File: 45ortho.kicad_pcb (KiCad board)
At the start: 2 copper layers, 266.7 x 95.2 mm, 158 parts

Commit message: a bit update (few routing, pro micro added, rotary added)
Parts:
- removed the REF** at (222.2, 146.1)
- removed the REF** at (210.3, 146.1)
- removed the REF** at (141.3, 146.1)
- removed the REF** at (117.5, 146.1)
- removed the REF** at (93.7, 146.1)
- removed the REF** at (138.9, 146.1)
- removed the REF** at (115.1, 146.1)
- removed the REF** at (91.3, 146.1)
- added D63: 1N4148W, Keebio-Parts:Diode-dual - Copy, B.Cu at (217.5, 146.1)
- added J1: ProMicro Extra Pin, Connector_PinSocket_2.54mm:PinSocket_1x02_P2.54mm_Vertical, B.Cu at (222.2, 144.8)
- added J2: USB Header, Connector_PinSocket_2.54mm:PinSocket_1x04_P2.54mm_Vertical, F.Cu at (151.8, 98.4)
- added MX63: MX-NoLED, MX_Only:MXOnly-1U-NoLED, F.Cu at (203.2, 146.1)
- added R1: 5.1k, Resistor_SMD:R_0603_1608Metric, B.Cu at (100.8, 88.9)
- added R2: 5.1k, Resistor_SMD:R_0603_1608Metric, B.Cu at (96.0, 88.9)
- added R3: 5.1k, Resistor_SMD:R_0603_1608Metric, B.Cu at (100.8, 69.8)
- added R4: 5.1k, Resistor_SMD:R_0603_1608Metric, B.Cu at (96.0, 69.8)
- added REF**: RotaryEncoder_EC11, Keebio-Parts:RotaryEncoder_EC11, B.Cu at (336.8, 69.8)
- added U3: ProMicro, Keebio-Parts:ArduinoProMicro-TopSide, B.Cu at (193.7, 146.1)
- added USB1: 6x14, Keebio-Parts:HRO-TYPE-C-31-M-12-Assembly, B.Cu at (98.4, 77.2)
- added USB2: 5x14, Keebio-Parts:HRO-TYPE-C-31-M-12-Assembly, B.Cu at (98.4, 57.9)
- MX62: footprint MX_Only:MXOnly-1U-NoLED -> MX_Only:MXOnly-6U-Centered-ReversedStabilizers-NoLED
- moved D61 30.7 mm to (214.3, 146.1), turned to 270 degrees
- moved D14 11.2 mm to (326.0, 71.5), turned to 270 degrees
- moved D62 9.69 mm to (211.1, 146.1), turned to 270 degrees
- moved MX62 9.52 mm to (193.7, 146.1)
- moved D59 7.94 mm to (127.0, 151.6)
- moved D44 1.40 mm to (108.0, 132.6)
- renumbered D63 to D64, D64 to D65, D65 to D66, D66 to D67, D67 to D68, D68 to D69, MX63 to MX64, MX64 to MX65, MX65 to MX66, MX66 to MX67, MX67 to MX68, MX68 to MX69
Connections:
- MX60 pad 1: col3 -> col4
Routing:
- net GND: track 0.00 -> 403.2 mm, vias 0 -> 2
- net row4: track 0.00 -> 311.4 mm
- net row1: track 0.00 -> 264.2 mm
- net row3: track 0.00 -> 263.2 mm
- net row2: track 0.00 -> 263.2 mm
- net D+: track 0.00 -> 177.5 mm, vias 0 -> 2
- net +5V: track 0.00 -> 167.5 mm, vias 0 -> 5
- net D-: track 0.00 -> 157.3 mm, vias 0 -> 2
- net col13: track 21.9 -> 112.8 mm
- net col8: track 21.8 -> 91.9 mm
- net col11: track 21.8 -> 82.1 mm
- net col12: track 21.8 -> 81.9 mm
- net col10: track 21.8 -> 81.8 mm
- net col9: track 21.8 -> 81.8 mm
- net col2: track 21.8 -> 81.8 mm
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- added copper zone on B.Cu, net GND
- added copper zone on F.Cu, net GND
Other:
- board text added: "+"
- board text added: "-"
- board text added: "G"
- board text added: "V"

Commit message: 99.99% final
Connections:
- J1 pad 1: (no net) -> row0
- U3 pad 1: (no net) -> col4
- U3 pad 10: (no net) -> col11
- U3 pad 11: (no net) -> col10
- U3 pad 12: (no net) -> col9
- U3 pad 13: (no net) -> row3
- U3 pad 14: (no net) -> row2
- U3 pad 15: (no net) -> row1
- U3 pad 16: (no net) -> row4
- U3 pad 17: (no net) -> col3
- U3 pad 18: (no net) -> col2
- U3 pad 19: (no net) -> col1
- U3 pad 2: (no net) -> col5
- U3 pad 20: (no net) -> col0
- U3 pad 5: (no net) -> col6
- U3 pad 6: (no net) -> col7
- U3 pad 7: (no net) -> col8
- U3 pad 8: (no net) -> col13
- U3 pad 9: (no net) -> col12
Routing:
- net col13: track 112.8 -> 259.3 mm
- net col12: track 81.9 -> 206.4 mm
- net col0: track 85.3 -> 198.4 mm
- net col11: track 82.1 -> 189.0 mm
- net row0: track 257.6 -> 360.4 mm, vias 0 -> 1
- net col1: track 81.8 -> 178.0 mm
- net col3: track 61.8 -> 145.3 mm
- net col10: track 81.8 -> 165.2 mm
- net row1: track 264.2 -> 346.0 mm, vias 0 -> 2
- net col2: track 81.8 -> 161.3 mm
- net row2: track 263.2 -> 327.5 mm, vias 0 -> 2
- net col9: track 81.8 -> 142.9 mm
- net col7: track 61.8 -> 112.6 mm
- net row3: track 263.2 -> 310.0 mm, vias 0 -> 1
- net col8: track 91.9 -> 128.1 mm
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
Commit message: bit of update
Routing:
- net GND: vias 19 -> 20
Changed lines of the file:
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@@
     (thickness 1.6)
     (drawings 8)
-    (tracks 972)
+    (tracks 973)
     (zones 0)
     (modules 162)
@@
     (add_net "Net-(D8-Pad2)")
     (add_net "Net-(D9-Pad2)")
-    (add_net "Net-(J1-Pad2)")
     (add_net "Net-(R1-Pad1)")
     (add_net "Net-(R2-Pad1)")
     (add_net "Net-(R3-Pad1)")
     (add_net "Net-(R4-Pad1)")
-    (add_net "Net-(U3-Pad21)")
-    (add_net "Net-(U3-Pad22)")
-    (add_net "Net-(U3-Pad24)")
-    (add_net "Net-(USB1-Pad3)")
-    (add_net "Net-(USB1-Pad9)")
-    (add_net "Net-(USB2-Pad3)")
-    (add_net "Net-(USB2-Pad9)")
     (add_net col0)
     (add_net col1)
@@
   (via (at 162.56 153.035) (size 0.8) (drill 0.4) (layers F.Cu B.Cu) (net 89))
   (via (at 224.409 146.05) (size 0.8) (drill 0.4) (layers F.Cu B.Cu) (net 89))
+  (via (at 214.3125 153.035) (size 0.8) (drill 0.4) (layers F.Cu B.Cu) (net 89))
   (segment (start 98.264999 83.826299) (end 99.099999 83.826299) (width 0.25) (layer B.Cu) (net 90))
   (segment (start 99.175 83.9013) (end 99.175 84.8763) (width 0.25) (layer B.Cu) (net 90))

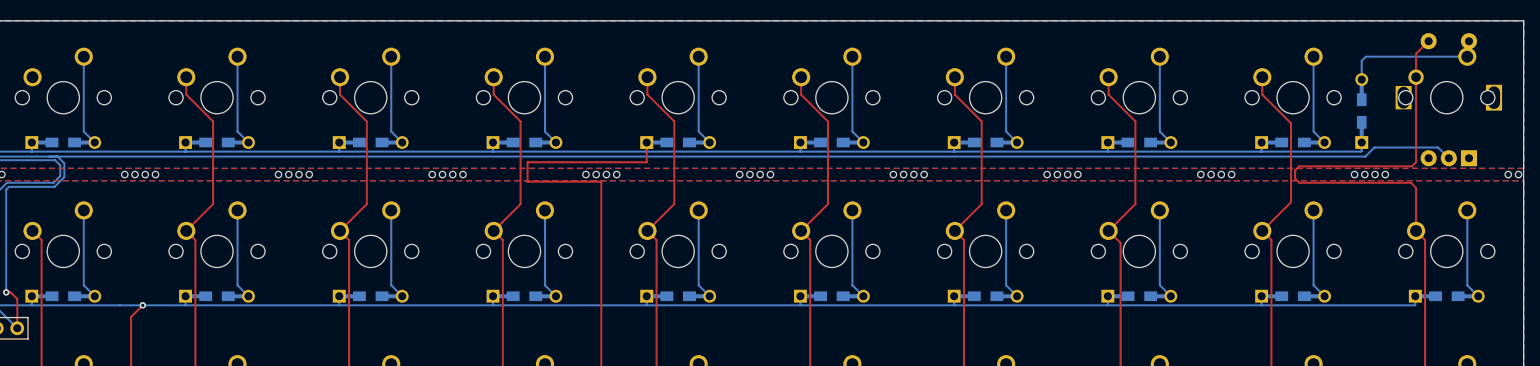
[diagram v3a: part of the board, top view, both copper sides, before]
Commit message: add 1 more encoder
no pin assigned, you still need to hand wire it directly to pro micro's mcu
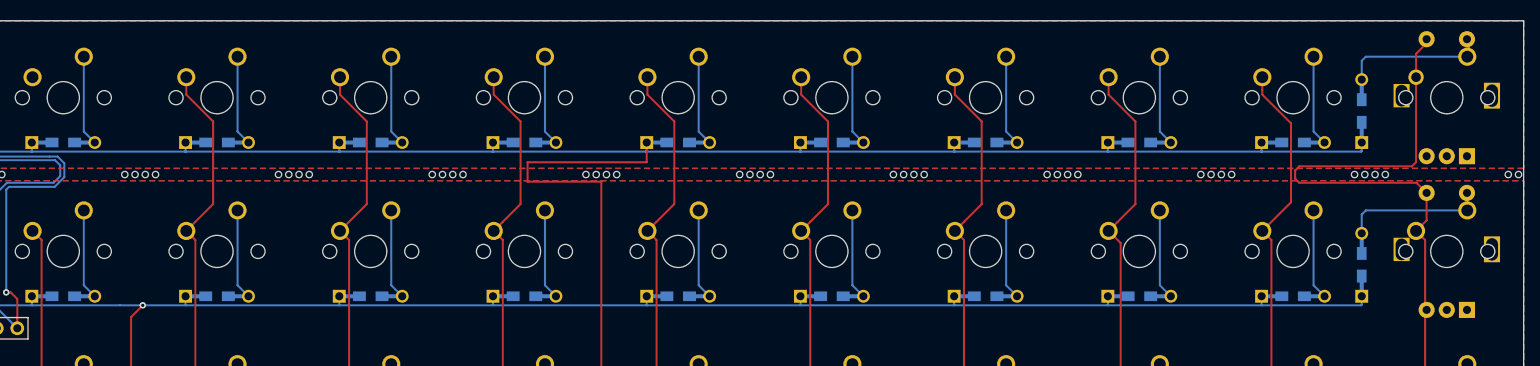
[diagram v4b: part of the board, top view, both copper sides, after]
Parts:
- added REF**: RotaryEncoder_EC11, Keebio-Parts:RotaryEncoder_EC11, B.Cu at (336.6, 88.7)
- moved D28 11.2 mm to (326.0, 90.6), turned to 270 degrees
- moved REF** 0.35 mm to (336.6, 69.6)
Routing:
- net GND: track 403.2 -> 228.7 mm
- net row1: track 346.0 -> 339.4 mm
- net Net-(D28-Pad2): track 11.2 -> 17.8 mm
- net col13: track 259.3 -> 260.8 mm
